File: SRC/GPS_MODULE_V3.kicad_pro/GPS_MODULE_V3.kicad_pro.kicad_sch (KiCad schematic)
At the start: 11 parts, among them J1 Input, J2 Conn_02x02_Odd_Even, Q1 SSM3J328R-HXY

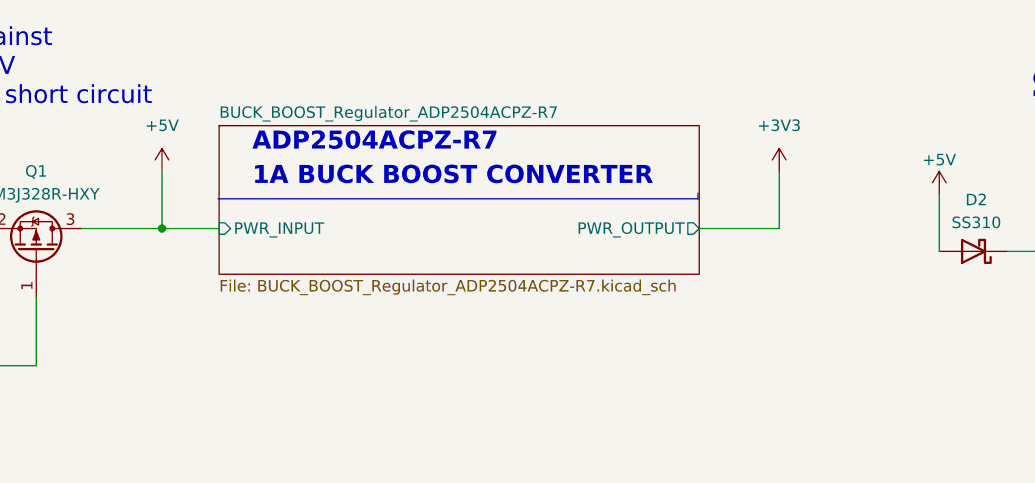
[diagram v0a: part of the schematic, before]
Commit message: gps update on buck 3v3
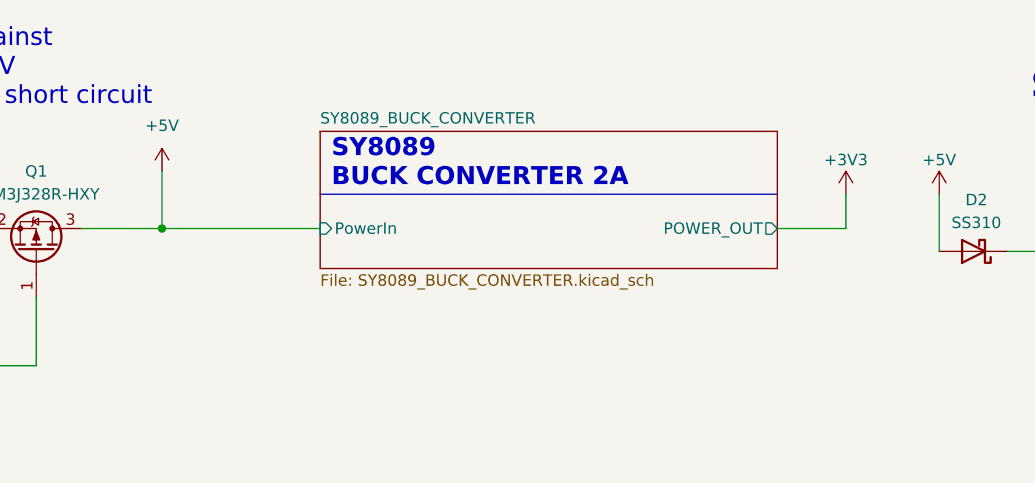
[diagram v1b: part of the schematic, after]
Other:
- removed sheet BUCK_BOOST_Regulator_ADP2504ACPZ-R7
- added sheet SY8089_BUCK_CONVERTER (SY8089_BUCK_CONVERTER.kicad_sch)
- note added: "SY8089 BUCK CONVERTER 2A"
- note removed: "1A BUCK BOOST CONVERTER"
- note removed: "ADP2504ACPZ-R7"
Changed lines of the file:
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@@
+    (stroke (width 0) (type default))
+  )
+  (polyline (pts (xy 130.0911 40.132) (xy 180.8911 40.132))
     (stroke (width 0) (type default))
   )
@@
     (stroke (width 0) (type default))
   )
-  (wire (pts (xy 112.522 43.942) (xy 118.872 43.942))
+  (wire (pts (xy 112.522 43.942) (xy 130.0911 43.942))
     (stroke (width 0) (type default))
   )
@@
     (stroke (width 0) (type default))
   )
-  (wire (pts (xy 181.102 43.942) (xy 172.212 43.942))
-    (stroke (width 0) (type default))
-  )
   (wire (pts (xy 82.042 36.322) (xy 82.042 43.942))
     (stroke (width 0) (type default))
   )
+  (wire (pts (xy 188.5111 40.132) (xy 188.5111 43.942))
+    (stroke (width 0) (type default))
+  )
   (wire (pts (xy 82.042 59.182) (xy 82.042 62.992))
     (stroke (width 0) (type default))
   )
-  (polyline (pts (xy 172.085 40.005) (xy 172.085 40.64))
-    (stroke (width 0) (type default))
-  )
   (wire (pts (xy 212.852 46.482) (xy 206.502 46.482))
     (stroke (width 0) (type default))
@@
     (stroke (width 0) (type default))
   )
-  (wire (pts (xy 181.102 37.592) (xy 181.102 43.942))
-    (stroke (width 0) (type default))
-  )
   (wire (pts (xy 160.02 89.535) (xy 186.69 89.535))
     (stroke (width 0) (type default))
@@
     (stroke (width 0) (type default))
   )
-  (polyline (pts (xy 118.745 40.64) (xy 172.085 40.64))
-    (stroke (width 0) (type default))
-  )
   (wire (pts (xy 237.617 46.482) (xy 240.03 46.482))
     (stroke (width 0) (type default))
@@
   )
   (wire (pts (xy 160.02 127.635) (xy 186.69 127.635))
+    (stroke (width 0) (type default))
+  )
+  (wire (pts (xy 180.8911 43.942) (xy 188.5111 43.942))
     (stroke (width 0) (type default))
   )
@@
     (effects (font (size 2 2) (thickness 0.4) bold) (justify left bottom))
   )
-  (text "ADP2504ACPZ-R7\n" (at 122.555 35.56 0)
-    (effects (font (size 2 2) (thickness 0.4) bold) (justify left bottom))
-  )
-  (text "1A BUCK BOOST CONVERTER" (at 122.555 39.37 0)
-    (effects (font (size 2 2) bold) (justify left bottom))
-  )
   (text "STM32FC8T6_MCU\n32BIT MCU F1" (at 123.19 83.82 0)
     (effects (font (size 2 2) (thickness 0.4) bold) (justify left bottom))
   )
   (text "MAX485\nRS485" (at 203.835 134.62 0)
+    (effects (font (size 2 2) (thickness 0.4) bold) (justify left bottom))
+  )
+  (text "SY8089\nBUCK CONVERTER 2A" (at 131.3611 39.497 0)
     (effects (font (size 2 2) (thickness 0.4) bold) (justify left bottom))
   )
@@
     (instances
       (project "GPS_MODULE_V3.kicad_pro"
-        (path "/8cb1db64-3fcc-4fb6-aa5a-7b4a50bb28df/e6086208-028a-42c2-b5d2-d48849fbb0ba"
-          (reference "R3") (unit 1)
-        )
         (path "/8cb1db64-3fcc-4fb6-aa5a-7b4a50bb28df"
           (reference "R1") (unit 1)
@@
     (instances
       (project "GPS_MODULE_V3.kicad_pro"
-        (path "/8cb1db64-3fcc-4fb6-aa5a-7b4a50bb28df/e6086208-028a-42c2-b5d2-d48849fbb0ba"
-          (reference "#PWR09") (unit 1)
-        )
         (path "/8cb1db64-3fcc-4fb6-aa5a-7b4a50bb28df"
           (reference "#PWR060") (unit 1)
@@
     (instances
       (project "GPS_MODULE_V3.kicad_pro"
-        (path "/8cb1db64-3fcc-4fb6-aa5a-7b4a50bb28df/e6086208-028a-42c2-b5d2-d48849fbb0ba"
-          (reference "#PWR09") (unit 1)
-        )
         (path "/8cb1db64-3fcc-4fb6-aa5a-7b4a50bb28df"
           (reference "#PWR02") (unit 1)
@@
     )
   )
-  (symbol (lib_id "power:+3V3") (at 181.102 37.592 0) (unit 1)
-    (in_bom yes) (on_board yes) (dnp no) (fields_autoplaced)
-    (property "Reference" "#PWR04" (at 181.102 41.402 0)
-      (effects (font (size 1.27 1.27)) hide)
-    )
-    (property "Value" "+3V3" (at 181.102 32.512 0)
-      (effects (font (size 1.27 1.27)))
-    )
-    (property "Footprint" "" (at 181.102 37.592 0)
-      (effects (font (size 1.27 1.27)) hide)
-    )
-    (property "Datasheet" "" (at 181.102 37.592 0)
+  (symbol (lib_id "power:+3V3") (at 188.5111 40.132 0) (unit 1)
+    (in_bom yes) (on_board yes) (dnp no) (fields_autoplaced)
+    (property "Reference" "#PWR04" (at 188.5111 43.942 0)
+      (effects (font (size 1.27 1.27)) hide)
+    )
+    (property "Value" "+3V3" (at 188.5111 36.322 0)
+      (effects (font (size 1.27 1.27)))
+    )
+    (property "Footprint" "" (at 188.5111 40.132 0)
+      (effects (font (size 1.27 1.27)) hide)
+    )
+    (property "Datasheet" "" (at 188.5111 40.132 0)
       (effects (font (size 1.27 1.27)) hide)
     )
@@
         (path "/8cb1db64-3fcc-4fb6-aa5a-7b4a50bb28df"
           (reference "#PWR04") (unit 1)
+        )
+      )
+      (project "BIM_PCB"
+        (path "/b79ebed7-e146-448b-8dab-0aefb3e182ca"
+          (reference "#PWR02") (unit 1)
         )
       )
@@
     (instances
       (project "GPS_MODULE_V3.kicad_pro"
-        (path "/8cb1db64-3fcc-4fb6-aa5a-7b4a50bb28df/e6086208-028a-42c2-b5d2-d48849fbb0ba"
-          (reference "#PWR010") (unit 1)
-        )
         (path "/8cb1db64-3fcc-4fb6-aa5a-7b4a50bb28df"
           (reference "#PWR01") (unit 1)
@@
     (instances
       (project "GPS_MODULE_V3.kicad_pro"
-        (path "/8cb1db64-3fcc-4fb6-aa5a-7b4a50bb28df/e6086208-028a-42c2-b5d2-d48849fbb0ba"
-          (reference "J1") (unit 1)
-        )
         (path "/8cb1db64-3fcc-4fb6-aa5a-7b4a50bb28df"
           (reference "J1") (unit 1)
@@
     (instances
       (project "GPS_MODULE_V3.kicad_pro"
-        (path "/8cb1db64-3fcc-4fb6-aa5a-7b4a50bb28df/e6086208-028a-42c2-b5d2-d48849fbb0ba"
-          (reference "TP2") (unit 1)
-        )
         (path "/8cb1db64-3fcc-4fb6-aa5a-7b4a50bb28df"
           (reference "TP1") (unit 1)
@@
     (instances
       (project "GPS_MODULE_V3.kicad_pro"
-        (path "/8cb1db64-3fcc-4fb6-aa5a-7b4a50bb28df/e6086208-028a-42c2-b5d2-d48849fbb0ba"
-          (reference "D1") (unit 1)
-        )
         (path "/8cb1db64-3fcc-4fb6-aa5a-7b4a50bb28df"
           (reference "D1") (unit 1)
@@
     )
   )
-  (sheet (at 118.872 32.512) (size 53.34 16.51) (fields_autoplaced)
+  (sheet (at 130.0911 33.147) (size 50.8 15.24) (fields_autoplaced)
     (stroke (width 0.1524) (type solid))
     (fill (color 255 255 0 1.0000))
-    (property "Sheetname" "BUCK_BOOST_Regulator_ADP2504ACPZ-R7" (at 118.872 31.8004 0)
+    (property "Sheetname" "SY8089_BUCK_CONVERTER" (at 130.0911 32.4354 0)
       (effects (font (size 1.27 1.27)) (justify left bottom))
     )
-    (property "Sheetfile" "BUCK_BOOST_Regulator_ADP2504ACPZ-R7.kicad_sch" (at 118.872 49.6066 0)
+    (property "Sheetfile" "SY8089_BUCK_CONVERTER.kicad_sch" (at 130.0911 48.9716 0)
       (effects (font (size 1.27 1.27)) (justify left top))
     )
-    (pin "PWR_OUTPUT" output (at 172.212 43.942 0)
-      (effects (font (size 1.27 1.27)) (justify right))
-    )
-    (pin "PWR_INPUT" input (at 118.872 43.942 180)
-      (effects (font (size 1.27 1.27)) (justify left))
-    )
-    (instances
+    (pin "POWER_OUT" output (at 180.8911 43.942 0)
+      (effects (font (size 1.27 1.27)) (justify right))
+    )
+    (pin "PowerIn" input (at 130.0911 43.942 180)
+      (effects (font (size 1.27 1.27)) (justify left))
+    )
+    (instances
+      (project "BIM_PCB"
+        (path "/b79ebed7-e146-448b-8dab-0aefb3e182ca" (page "18"))
+      )
       (project "GPS_MODULE_V3.kicad_pro"
         (path "/8cb1db64-3fcc-4fb6-aa5a-7b4a50bb28df" (page "2"))

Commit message: BOM updates
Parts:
- renumbered R3 to R1, TP2 to TP1
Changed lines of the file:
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@@
   (symbol (lib_id "Device:R_US") (at 82.042 66.802 0) (unit 1)
     (in_bom yes) (on_board yes) (dnp no) (fields_autoplaced)
-    (property "Reference" "R3" (at 84.582 66.167 0)
+    (property "Reference" "R1" (at 84.582 66.167 0)
       (effects (font (size 1.27 1.27)) (justify left))
     )
@@
   (symbol (lib_id "power:GND") (at 255.905 136.525 0) (unit 1)
     (in_bom yes) (on_board yes) (dnp no) (fields_autoplaced)
-    (property "Reference" "#PWR09" (at 255.905 142.875 0)
+    (property "Reference" "#PWR060" (at 255.905 142.875 0)
       (effects (font (size 1.27 1.27)) hide)
     )
@@
   (symbol (lib_id "power:GND") (at 82.042 79.502 0) (unit 1)
     (in_bom yes) (on_board yes) (dnp no) (fields_autoplaced)
-    (property "Reference" "#PWR09" (at 82.042 85.852 0)
+    (property "Reference" "#PWR02" (at 82.042 85.852 0)
       (effects (font (size 1.27 1.27)) hide)
     )
@@
   (symbol (lib_id "power:GND") (at 46.482 51.562 0) (unit 1)
     (in_bom yes) (on_board yes) (dnp no) (fields_autoplaced)
-    (property "Reference" "#PWR010" (at 46.482 57.912 0)
+    (property "Reference" "#PWR01" (at 46.482 57.912 0)
       (effects (font (size 1.27 1.27)) hide)
     )
@@
   (symbol (lib_id "Connector:TestPoint") (at 82.042 36.322 0) (unit 1)
     (in_bom yes) (on_board yes) (dnp no) (fields_autoplaced)
-    (property "Reference" "TP2" (at 84.582 32.385 0)
+    (property "Reference" "TP1" (at 84.582 32.385 0)
       (effects (font (size 1.27 1.27)) (justify left))
     )

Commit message: updates on BOM, CPL and gerbers
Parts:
- removed J2: Conn_02x02_Odd_Even, Connector_Molex:Molex_Nano-Fit_105314-xx04_2x02_P2.50mm_Horizontal, symbol Connector_Generic:Conn_02x02_Odd_Even
- added J2: Conn_02x04_Odd_Even, Connector_Molex:Molex_Mini-Fit_Jr_5569-08A2_2x04_P4.20mm_Horizontal, symbol Connector_Generic:Conn_02x04_Odd_Even
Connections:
- net +5V: now also J2.2 (Pin_2)
- net GND: now also J2.1 (Pin_1), J2.7 (Pin_7)
- net RS485_MAX485/A: now also J2.3 (Pin_3)
- net RS485_MAX485/B: now also J2.5 (Pin_5)
- new net STM32F103C8T6_MCU/SW0: J2.4 (Pin_4)
- new net STM32F103C8T6_MCU/swdclk: J2.8 (Pin_8)
- new net STM32F103C8T6_MCU/swdio: J2.6 (Pin_6)
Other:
- removed sheet SIM7000E_GPRS_SIM MODULE
- added sheet A9G_GSM_GPRS_MODULE (A9G_GSM_GPRS_MODULE.kicad_sch)
- sheet STM32F103C8T6_MCU ports: added SW0, swdclk, swdio; removed none
- note added: "A9G GPRS MODULE WITH GPS"
- note removed: "SIM7000E GPRS MODULE WITH GPS"

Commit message: routing
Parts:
- removed J2: Conn_02x04_Odd_Even, Connector_Molex:Molex_Mini-Fit_Jr_5569-08A2_2x04_P4.20mm_Horizontal, symbol Connector_Generic:Conn_02x04_Odd_Even
- added J5: Conn_02x06_Counter_Clockwise, MACHADA_footprints:auto_jae_conn_02x06_p2.5mm_MX23A12NF1, symbol Connector_Generic:Conn_02x06_Counter_Clockwise
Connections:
- net +5V: now also J5.12 (Pin_12)
- net GND: now also J5.1 (Pin_1), J5.4 (Pin_4), J5.5 (Pin_5), J5.6 (Pin_6), J5.7 (Pin_7), J5.8 (Pin_8)
- net RS485_MAX485/A: now also J5.2 (Pin_2)
- net RS485_MAX485/B: now also J5.3 (Pin_3)
- net STM32F103C8T6_MCU/SW0: now also J5.11 (Pin_11)
- net STM32F103C8T6_MCU/swdclk: now also J5.9 (Pin_9)
- net STM32F103C8T6_MCU/swdio: now also J5.10 (Pin_10)
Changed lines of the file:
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@@
 (kicad_sch (version 20230121) (generator eeschema)
   (paper "A4")
+  (junction (at 238.76 140.335) (diameter 0) (color 0 0 0 0)
+  )
   (junction (at 82.042 59.182) (diameter 0) (color 0 0 0 0)
   )
   (junction (at 82.042 43.942) (diameter 0) (color 0 0 0 0)
   )
+  (junction (at 238.76 137.795) (diameter 0) (color 0 0 0 0)
+  )
   (junction (at 112.522 43.942) (diameter 0) (color 0 0 0 0)
   )
+  (junction (at 251.46 140.335) (diameter 0) (color 0 0 0 0)
+  )
   (junction (at 240.03 46.482) (diameter 0) (color 0 0 0 0)
   )
@@
     (stroke (width 0) (type default))
   )
+  (wire (pts (xy 251.46 135.255) (xy 259.715 135.255))
+    (stroke (width 0) (type default))
+  )
   (wire (pts (xy 260.35 124.46) (xy 260.35 127.635))
     (stroke (width 0) (type default))
@@
     (stroke (width 0) (type default))
   )
+  (wire (pts (xy 251.46 132.715) (xy 263.525 132.715))
+    (stroke (width 0) (type default))
+  )
   (polyline (pts (xy 115.57 85.725) (xy 160.02 85.725))
     (stroke (width 0) (type default))
@@
     (stroke (width 0) (type default))
   )
+  (wire (pts (xy 238.76 137.795) (xy 238.76 140.335))
+    (stroke (width 0) (type default))
+  )
   (wire (pts (xy 160.02 149.225) (xy 263.525 149.225))
     (stroke (width 0) (type default))
@@
     (stroke (width 0) (type default))
   )
+  (wire (pts (xy 160.02 110.49) (xy 186.69 110.49))
+    (stroke (width 0) (type default))
+  )
+  (wire (pts (xy 229.235 123.19) (xy 229.235 120.65))
+    (stroke (width 0) (type default))
+  )
   (wire (pts (xy 251.46 130.175) (xy 266.7 130.175))
     (stroke (width 0) (type default))
   )
-  (wire (pts (xy 160.02 110.49) (xy 186.69 110.49))
-    (stroke (width 0) (type default))
-  )
-  (wire (pts (xy 229.235 123.19) (xy 229.235 120.65))
-    (stroke (width 0) (type default))
-  )
   (wire (pts (xy 82.042 36.322) (xy 82.042 43.942))
     (stroke (width 0) (type default))
@@
     (stroke (width 0) (type default))
   )
+  (wire (pts (xy 238.76 140.335) (xy 238.76 140.97))
+    (stroke (width 0) (type default))
+  )
   (wire (pts (xy 82.042 59.182) (xy 82.042 62.992))
     (stroke (width 0) (type default))
@@
     (stroke (width 0) (type default))
   )
+  (wire (pts (xy 251.46 140.335) (xy 251.46 141.605))
+    (stroke (width 0) (type default))
+  )
   (wire (pts (xy 212.852 46.482) (xy 206.502 46.482))
     (stroke (width 0) (type default))
@@
     (stroke (width 0) (type default))
   )
+  (wire (pts (xy 251.46 137.795) (xy 251.46 140.335))
+    (stroke (width 0) (type default))
+  )
   (wire (pts (xy 82.042 70.612) (xy 82.042 79.502))
     (stroke (width 0) (type default))
@@
     (stroke (width 0) (type default))
   )
-  (wire (pts (xy 238.76 135.255) (xy 236.855 135.255))
-    (stroke (width 0) (type default))
-  )
   (wire (pts (xy 98.552 59.182) (xy 82.042 59.182))
     (stroke (width 0) (type default))
@@
     (stroke (width 0) (type default))
   )
-  (wire (pts (xy 263.525 132.715) (xy 251.46 132.715))
-    (stroke (width 0) (type default))
-  )
   (wire (pts (xy 83.82 132.715) (xy 115.57 132.715))
     (stroke (width 0) (type default))
@@
     (stroke (width 0) (type default))
   )
-  (wire (pts (xy 236.855 135.255) (xy 236.855 137.16))
+  (wire (pts (xy 238.76 135.255) (xy 238.76 137.795))
     (stroke (width 0) (type default))
   )
@@
     (stroke (width 0) (type default))
   )
+  (wire (pts (xy 251.46 127.635) (xy 260.35 127.635))
+    (stroke (width 0) (type default))
+  )
   (wire (pts (xy 83.82 111.125) (xy 115.57 111.125))
     (stroke (width 0) (type default))
   )
-  (wire (pts (xy 260.35 127.635) (xy 251.46 127.635))
-    (stroke (width 0) (type default))
-  )
   (wire (pts (xy 259.715 146.685) (xy 259.715 135.255))
-    (stroke (width 0) (type default))
-  )
-  (wire (pts (xy 259.715 135.255) (xy 251.46 135.255))
     (stroke (width 0) (type default))
   )
@@
     )
   )
-  (symbol (lib_id "Connector_Generic:Conn_02x04_Odd_Even") (at 243.84 130.175 0) (unit 1)
-    (in_bom yes) (on_board yes) (dnp no) (fields_autoplaced)
-    (property "Reference" "J2" (at 245.11 121.92 0)
-      (effects (font (size 1.27 1.27)))
-    )
-    (property "Value" "Conn_02x04_Odd_Even" (at 245.11 124.46 0)
-      (effects (font (size 1.27 1.27)))
-    )
-    (property "Footprint" "Connector_Molex:Molex_Mini-Fit_Jr_5569-08A2_2x04_P4.20mm_Horizontal" (at 243.84 130.175 0)
-      (effects (font (size 1.27 1.27)) hide)
-    )
-    (property "Datasheet" "~" (at 243.84 130.175 0)
-      (effects (font (size 1.27 1.27)) hide)
-    )
-    (pin "1")
-    (pin "2")
-    (pin "3")
-    (pin "4")
-    (pin "5")
-    (pin "6")
-    (pin "7")
-    (pin "8")
-    (instances
-      (project "GPS_MODULE_V3.kicad_pro"
-        (path "/8cb1db64-3fcc-4fb6-aa5a-7b4a50bb28df"
-          (reference "J2") (unit 1)
-        )
-      )
-    )
-  )
   (symbol (lib_id "Device:R_US") (at 82.042 66.802 0) (unit 1)
     (in_bom yes) (on_board yes) (dnp no) (fields_autoplaced)
@@
     )
   )
+  (symbol (lib_id "power:GND") (at 251.46 141.605 0) (unit 1)
+    (in_bom yes) (on_board yes) (dnp no)
+    (property "Reference" "#PWR023" (at 251.46 147.955 0)
+      (effects (font (size 1.27 1.27)) hide)
+    )
+    (property "Value" "GND" (at 251.46 145.415 0)
+      (effects (font (size 1.27 1.27)))
+    )
+    (property "Footprint" "" (at 251.46 141.605 0)
+      (effects (font (size 1.27 1.27)) hide)
+    )
+    (property "Datasheet" "" (at 251.46 141.605 0)
+      (effects (font (size 1.27 1.27)) hide)
+    )
+    (pin "1")
+    (instances
+      (project "GPS_MODULE_V3.kicad_pro"
+        (path "/8cb1db64-3fcc-4fb6-aa5a-7b4a50bb28df"
+          (reference "#PWR023") (unit 1)
+        )
+      )
+    )
+  )
+  (symbol (lib_id "Connector_Generic:Conn_02x06_Counter_Clockwise") (at 243.84 132.715 0) (unit 1)
+    (in_bom yes) (on_board yes) (dnp no)
+    (property "Reference" "J5" (at 245.11 121.92 0)
+      (effects (font (size 1.27 1.27)))
+    )
+    (property "Value" "Conn_02x06_Counter_Clockwise" (at 245.11 124.46 0)
+      (effects (font (size 1.27 1.27)))
+    )
+    (property "Footprint" "MACHADA_footprints:auto_jae_conn_02x06_p2.5mm_MX23A12NF1" (at 243.84 132.715 0)
+      (effects (font (size 1.27 1.27)) hide)
+    )
+    (property "Datasheet" "~" (at 243.84 132.715 0)
+      (effects (font (size 1.27 1.27)) hide)
+    )
+    (property "MPN" "MX23A12NF1" (at 244.475 120.015 0)
+      (effects (font (size 1.27 1.27)))
+    )
+    (pin "1")
+    (pin "7")
+    (pin "10")
+    (pin "2")
+    (pin "8")
+    (pin "6")
+    (pin "12")
+    (pin "5")
+    (pin "11")
+    (pin "9")
+    (pin "4")
+    (pin "3")
+    (instances
+      (project "GPS_MODULE_V3.kicad_pro"
+        (path "/8cb1db64-3fcc-4fb6-aa5a-7b4a50bb28df"
+          (reference "J5") (unit 1)
+        )
+      )
+    )
+  )
   (symbol (lib_id "Device:D_Schottky") (at 233.807 46.482 180) (unit 1)
     (in_bom yes) (on_board yes) (dnp no) (fields_autoplaced)
@@
     )
   )
-  (symbol (lib_id "power:GND") (at 236.855 137.16 0) (unit 1)
-    (in_bom yes) (on_board yes) (dnp no) (fields_autoplaced)
-    (property "Reference" "#PWR058" (at 236.855 143.51 0)
-      (effects (font (size 1.27 1.27)) hide)
-    )
-    (property "Value" "GND" (at 236.855 142.24 0)
-      (effects (font (size 1.27 1.27)))
-    )
-    (property "Footprint" "" (at 236.855 137.16 0)
-      (effects (font (size 1.27 1.27)) hide)
-    )
-    (property "Datasheet" "" (at 236.855 137.16 0)
-      (effects (font (size 1.27 1.27)) hide)
-    )
+  (symbol (lib_id "power:GND") (at 238.76 140.97 0) (unit 1)
+    (in_bom yes) (on_board yes) (dnp no)
+    (property "Reference" "#PWR058" (at 238.76 147.32 0)
+      (effects (font (size 1.27 1.27)) hide)
+    )
+    (property "Value" "GND" (at 238.76 144.78 0)
+      (effects (font (size 1.27 1.27)))
+    )
+    (property "Footprint" "" (at 238.76 140.97 0)
+      (effects (font (size 1.27 1.27)) hide)
+    )
+    (property "Datasheet" "" (at 238.76 140.97 0)
+      (effects (font (size 1.27 1.27)) hide)
+    )

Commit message: completed GPS ecoboda files
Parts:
- removed J1: Input, TerminalBlock_Phoenix:TerminalBlock_Phoenix_PT-1,5-2-3.5-H_1x02_P3.50mm_Horizontal, symbol Connector:Screw_Terminal_01x02
- D2: value SS310 -> RS1K-E3/5AT; MPN (none) -> RS1K-E3/5AT
- D3, D4: value SS310 -> RS1K-E3/5AT
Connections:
- net +5V: now also TH1.1; no longer D2.2 (A), Q1.3 (D)
- new net 5V_FILTERED_: D2.2 (A), Q1.3 (D)
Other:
- moved on the sheet: D2, D3, D4, SIM_PWR1

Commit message: GPS all files BOM and placemnt guide files added
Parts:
- TH1: footprint Fuse:Fuse_0603_1608Metric_Pad1.05x0.95mm_HandSolder -> Fuse:Fuse_1206_3216Metric; MPN PRG18BC1R0MM1RB -> ASMD1206-100
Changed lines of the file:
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@@
     )
     (pin "1")
+    (pin "10")
+    (pin "11")
+    (pin "12")
+    (pin "2")
+    (pin "3")
+    (pin "4")
+    (pin "5")
+    (pin "6")
     (pin "7")
-    (pin "10")
-    (pin "2")
     (pin "8")
-    (pin "6")
-    (pin "12")
-    (pin "5")
-    (pin "11")
     (pin "9")
-    (pin "4")
-    (pin "3")
     (instances
       (project "GPS_MODULE_V3.kicad_pro"
@@
       (effects (font (size 1.27 1.27)))
     )
-    (property "Footprint" "Fuse:Fuse_0603_1608Metric_Pad1.05x0.95mm_HandSolder" (at 71.882 42.672 0)
+    (property "Footprint" "Fuse:Fuse_1206_3216Metric" (at 71.882 42.672 0)
       (effects (font (size 1.27 1.27)) (justify left) hide)
     )
@@
       (effects (font (size 1.27 1.27)) hide)
     )
-    (property "MPN" "PRG18BC1R0MM1RB" (at 66.802 47.752 90)
+    (property "MPN" "ASMD1206-100" (at 66.802 47.752 90)
       (effects (font (size 1.27 1.27)))
     )
